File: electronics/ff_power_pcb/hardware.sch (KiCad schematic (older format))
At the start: 60 parts, among them J1 Conn_01x01_Female, J2 Conn_01x01_Female, J3 Conn_01x07_Male, U3 TPS62095RGTR, U4 TPS62095RGTR, U5 TPS62095RGTR, U6 TPS62095RGTR, U7 AP131-25

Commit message: Working on the electronics for the FF revision.
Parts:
- CY3: renamed from C3; footprint (none) -> Capacitor_THT:C_Disc_D7.5mm_W5.0mm_P10.00mm; MPN (none) -> C901U102MUVDBA7317
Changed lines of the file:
@@
 AR Path="/60536DA4/60E826A4" Ref="C?"  Part="1"
 AR Path="/60A30BFF/60E826A4" Ref="C?"  Part="1"
-AR Path="/60E826A4" Ref="C3"  Part="1"
-F 0 "C3" V 7950 2700 50  0000 L CNN
+AR Path="/60E826A4" Ref="CY3"  Part="1"
+F 0 "CY3" V 7950 2700 50  0000 L CNN
 F 1 "1.0nF" V 7900 3050 50  0000 C CNN
-F 2 "" H 8050 2850 50  0001 C CNN
+F 2 "Capacitor_THT:C_Disc_D7.5mm_W5.0mm_P10.00mm" H 8050 2850 50  0001 C CNN
 F 3 "~" H 8050 2850 50  0001 C CNN
-F 4 "" H 8100 3050 50  0001 C CNN "MPN"
+F 4 "C901U102MUVDBA7317" H 8100 3050 50  0001 C CNN "MPN"
 F 5 "~" H 8100 3050 50  0001 C CNN "Tolerance"
 F 6 "400Vac" V 8000 3050 50  0000 C CNN "Voltage"

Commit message: Added step files, Working on the power board.
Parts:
- F1: footprint Fuse:Fuse_Littelfuse-NANO2-451_453 -> Fuse:Fuse_Littelfuse_395Series; MPN 0679H1000-01 -> 36911000000
- J1, J2: footprint Connector_PinHeader_2.54mm:PinHeader_1x01_P2.54mm_Vertical -> mains_blade:IRL_00
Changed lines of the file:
@@
 F 0 "F1" V 5153 1950 50  0000 C CNN
 F 1 "1A/300V Slow" V 5244 1950 50  0000 C CNN
-F 2 "Fuse:Fuse_Littelfuse-NANO2-451_453" V 5280 1950 50  0001 C CNN
+F 2 "Fuse:Fuse_Littelfuse_395Series" V 5280 1950 50  0001 C CNN
 F 3 "~" H 5350 1950 50  0001 C CNN
-F 4 "0679H1000-01" V 5350 1950 50  0001 C CNN "MPN"
+F 4 "36911000000" V 5350 1950 50  0001 C CNN "MPN"
 	1    5350 1950
 	0    1    1    0
@@
 F 0 "J1" H 4142 2317 50  0000 C CNN
 F 1 "Conn_01x01_Female" H 4142 2316 50  0001 C CNN
-F 2 "Connector_PinHeader_2.54mm:PinHeader_1x01_P2.54mm_Vertical" H 4250 2450 50  0001 C CNN
+F 2 "mains_blade:IRL_00" H 4250 2450 50  0001 C CNN
 F 3 "~" H 4250 2450 50  0001 C CNN
 	1    4250 2450
@@
 F 0 "J2" H 4142 1817 50  0000 C CNN
 F 1 "Conn_01x01_Female" H 4142 1816 50  0001 C CNN
-F 2 "Connector_PinHeader_2.54mm:PinHeader_1x01_P2.54mm_Vertical" H 4250 1950 50  0001 C CNN
+F 2 "mains_blade:IRL_00" H 4250 1950 50  0001 C CNN
 F 3 "~" H 4250 1950 50  0001 C CNN
 	1    4250 1950

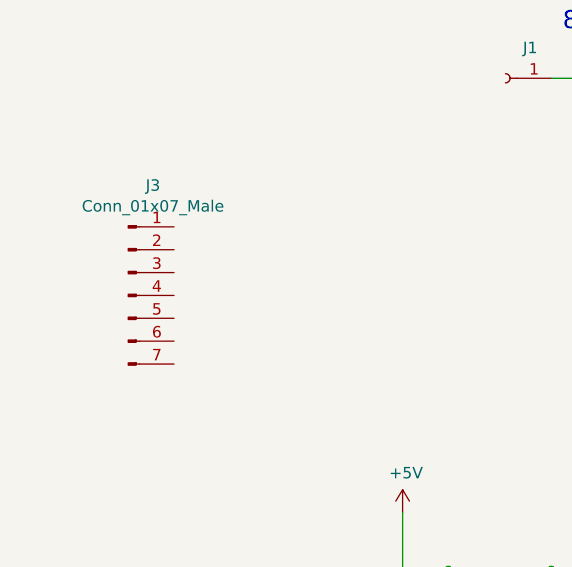
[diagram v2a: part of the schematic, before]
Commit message: Finished up the routing on the power board, still needs a double check.
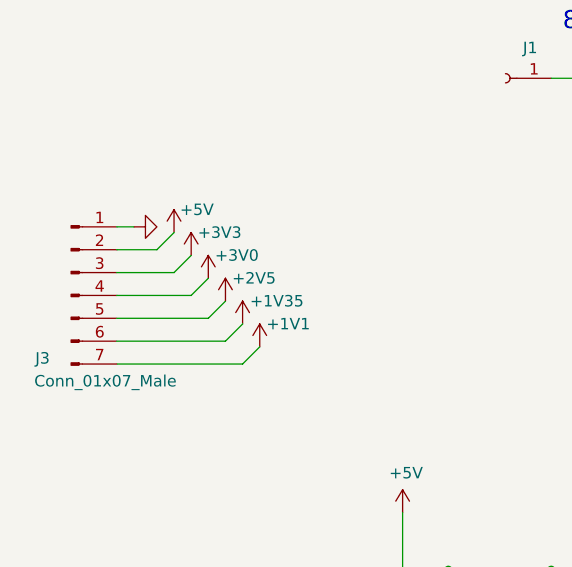
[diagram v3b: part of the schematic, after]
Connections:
- net +1V1: now also J3.7 (Pin_7)
- net +1V35: now also J3.6 (Pin_6)
- net +2V5: now also J3.5 (Pin_5)
- net +3V0: now also J3.4 (Pin_4)
- net +3V3: now also J3.3 (Pin_3)
- net +5V: now also J3.2 (Pin_2)
- net GND: now also J3.1 (Pin_1)
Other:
- moved on the sheet: J3
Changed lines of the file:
@@
 L Connector:Conn_01x07_Male J3
 U 1 1 60CBBBFE
-P 2600 3400
-F 0 "J3" H 2708 3881 50  0000 C CNN
-F 1 "Conn_01x07_Male" H 2708 3790 50  0000 C CNN
-F 2 "Connector_PinSocket_2.54mm:PinSocket_1x07_P2.54mm_Vertical" H 2600 3400 50  0001 C CNN
-F 3 "~" H 2600 3400 50  0001 C CNN
-	1    2600 3400
+P 2350 3400
+F 0 "J3" H 2225 3125 50  0000 C CNN
+F 1 "Conn_01x07_Male" H 2500 3025 50  0000 C CNN
+F 2 "Connector_PinSocket_2.54mm:PinSocket_1x07_P2.54mm_Vertical" H 2350 3400 50  0001 C CNN
+F 3 "~" H 2350 3400 50  0001 C CNN
+	1    2350 3400
 	1    0    0    -1
 $EndComp
@@
 Wire Wire Line
 	7050 1950 7450 1950
+Wire Wire Line
+	2550 3700 3100 3700
+Wire Wire Line
+	3100 3700 3175 3625
+$Comp
+L power:+1V35 #PWR?
+U 1 1 61108D89
+P 3100 3525
+AR Path="/60536DA4/61108D89" Ref="#PWR?"  Part="1"
+AR Path="/60A30BFF/61108D89" Ref="#PWR?"  Part="1"
+AR Path="/61108D89" Ref="#PWR?"  Part="1"
+F 0 "#PWR?" H 3100 3375 50  0001 C CNN
+F 1 "+1V35" H 3250 3625 50  0000 C CNN
+F 2 "" H 3100 3525 50  0001 C CNN
+F 3 "" H 3100 3525 50  0001 C CNN
+	1    3100 3525
+	1    0    0    -1
+$EndComp
+$Comp
+L power:+5V #PWR?
+U 1 1 6110AA8A
+P 2800 3125
+F 0 "#PWR?" H 2800 2975 50  0001 C CNN
+F 1 "+5V" H 2900 3225 50  0000 C CNN
+F 2 "" H 2800 3125 50  0001 C CNN
+F 3 "" H 2800 3125 50  0001 C CNN
+	1    2800 3125
+	1    0    0    -1
+$EndComp
+$Comp
+L power:+3V0 #PWR?
+U 1 1 6110CD65
+P 2950 3325
+F 0 "#PWR?" H 2950 3175 50  0001 C CNN
+F 1 "+3V0" H 3075 3425 50  0000 C CNN
+F 2 "" H 2950 3325 50  0001 C CNN
+F 3 "" H 2950 3325 50  0001 C CNN
+	1    2950 3325
+	1    0    0    -1
+$EndComp
+$Comp
+L power:+1V1 #PWR?
+U 1 1 611106CE
+P 3175 3625
+F 0 "#PWR?" H 3175 3475 50  0001 C CNN
+F 1 "+1V1" H 3300 3725 50  0000 C CNN
+F 2 "" H 3175 3625 50  0001 C CNN
+F 3 "" H 3175 3625 50  0001 C CNN
+	1    3175 3625
+	1    0    0    -1
+$EndComp
+$Comp
+L power:+2V5 #PWR?
+U 1 1 61112D49
+P 3025 3425
+F 0 "#PWR?" H 3025 3275 50  0001 C CNN
+F 1 "+2V5" H 3150 3525 50  0000 C CNN
+F 2 "" H 3025 3425 50  0001 C CNN
+F 3 "" H 3025 3425 50  0001 C CNN
+	1    3025 3425
+	1    0    0    -1
+$EndComp
+Wire Wire Line
+	2550 3600 3025 3600
+Wire Wire Line
+	3025 3600 3100 3525
+Wire Wire Line
+	2550 3500 2950 3500
+Wire Wire Line
+	2950 3500 3025 3425
+Wire Wire Line
+	2550 3400 2875 3400
+Wire Wire Line
+	2875 3400 2950 3325
+Wire Wire Line
+	2550 3300 2800 3300
+Wire Wire Line
+	2800 3300 2875 3225
+$Comp
+L power:+3V3 #PWR?
+U 1 1 61107094
+P 2875 3225
+F 0 "#PWR?" H 2875 3075 50  0001 C CNN
+F 1 "+3V3" H 3000 3325 50  0000 C CNN
+F 2 "" H 2875 3225 50  0001 C CNN
+F 3 "" H 2875 3225 50  0001 C CNN
+	1    2875 3225
+	1    0    0    -1
+$EndComp
+Wire Wire Line
+	2550 3200 2725 3200
+Wire Wire Line
+	2725 3200 2800 3125
+$Comp
+L power:GND #PWR?
+U 1 1 61381F70
+P 2625 3100
+AR Path="/60536DA4/61381F70" Ref="#PWR?"  Part="1"
+AR Path="/60A30BFF/61381F70" Ref="#PWR?"  Part="1"
+AR Path="/61381F70" Ref="#PWR?"  Part="1"
+F 0 "#PWR?" H 2625 2850 50  0001 C CNN
+F 1 "GND" V 2630 2972 50  0001 R CNN
+F 2 "" H 2625 3100 50  0001 C CNN
+F 3 "" H 2625 3100 50  0001 C CNN
+	1    2625 3100
+	0    -1   -1   0
+$EndComp
+Wire Wire Line
+	2625 3100 2550 3100
 $EndSCHEMATC

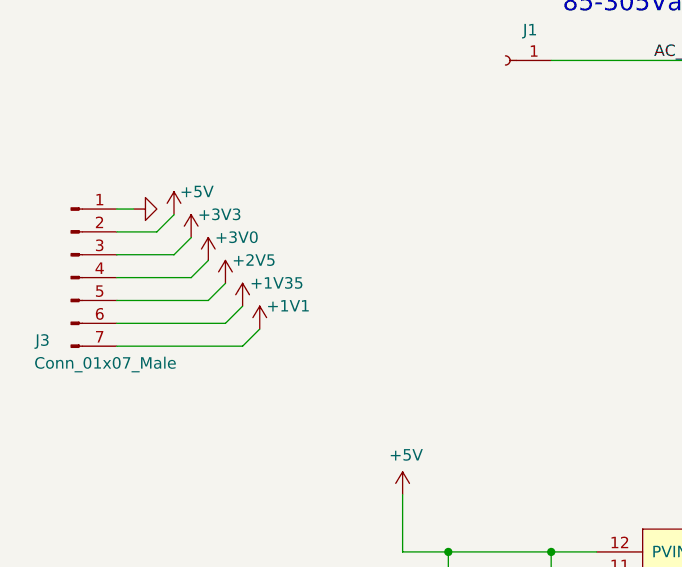
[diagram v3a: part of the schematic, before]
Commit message: Rerouted the power traces for R0.1 power pcb - they didn't match the compute PCB power pins.
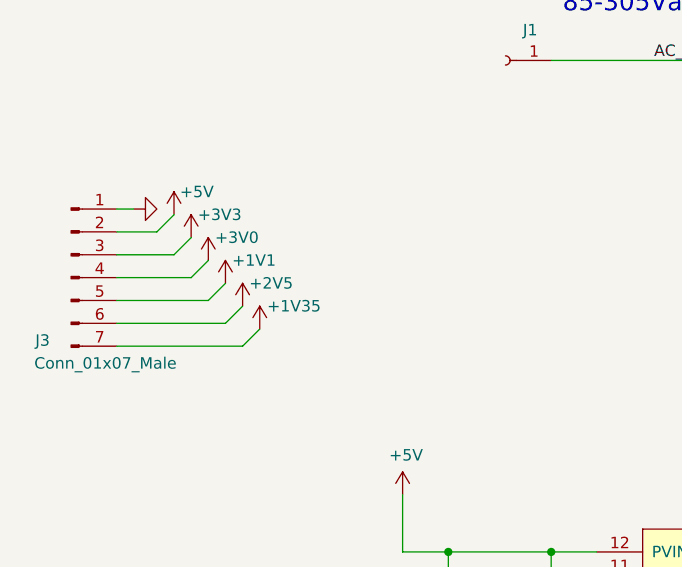
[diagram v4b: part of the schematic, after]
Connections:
- net +1V1: now also J3.5 (Pin_5); no longer J3.7 (Pin_7)
- net +1V35: now also J3.7 (Pin_7); no longer J3.6 (Pin_6)
- net +2V5: now also J3.6 (Pin_6); no longer J3.5 (Pin_5)
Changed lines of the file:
@@
 L power:+1V35 #PWR?
 U 1 1 61108D89
-P 3100 3525
+P 3175 3625
 AR Path="/60536DA4/61108D89" Ref="#PWR?"  Part="1"
 AR Path="/60A30BFF/61108D89" Ref="#PWR?"  Part="1"
 AR Path="/61108D89" Ref="#PWR?"  Part="1"
-F 0 "#PWR?" H 3100 3375 50  0001 C CNN
-F 1 "+1V35" H 3250 3625 50  0000 C CNN
-F 2 "" H 3100 3525 50  0001 C CNN
-F 3 "" H 3100 3525 50  0001 C CNN
-	1    3100 3525
+F 0 "#PWR?" H 3175 3475 50  0001 C CNN
+F 1 "+1V35" H 3325 3725 50  0000 C CNN
+F 2 "" H 3175 3625 50  0001 C CNN
+F 3 "" H 3175 3625 50  0001 C CNN
+	1    3175 3625
 	1    0    0    -1
 $EndComp
@@
 L power:+1V1 #PWR?
 U 1 1 611106CE
-P 3175 3625
-F 0 "#PWR?" H 3175 3475 50  0001 C CNN
-F 1 "+1V1" H 3300 3725 50  0000 C CNN
-F 2 "" H 3175 3625 50  0001 C CNN
-F 3 "" H 3175 3625 50  0001 C CNN
-	1    3175 3625
-	1    0    0    -1
-$EndComp
-$Comp
-L power:+2V5 #PWR?
-U 1 1 61112D49
 P 3025 3425
 F 0 "#PWR?" H 3025 3275 50  0001 C CNN
-F 1 "+2V5" H 3150 3525 50  0000 C CNN
+F 1 "+1V1" H 3150 3525 50  0000 C CNN
 F 2 "" H 3025 3425 50  0001 C CNN
 F 3 "" H 3025 3425 50  0001 C CNN
@@
 Wire Wire Line
 	2625 3100 2550 3100
+$Comp
+L power:+2V5 #PWR?
+U 1 1 61112D49
+P 3100 3525
+F 0 "#PWR?" H 3100 3375 50  0001 C CNN
+F 1 "+2V5" H 3225 3625 50  0000 C CNN
+F 2 "" H 3100 3525 50  0001 C CNN
+F 3 "" H 3100 3525 50  0001 C CNN
+	1    3100 3525
+	1    0    0    -1
+$EndComp
 $EndSCHEMATC

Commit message: Updated the regulator to the proper value.
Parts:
- U7: value AP131-25 -> AP131-33; symbol Regulator_Linear:AP131-25 -> Regulator_Linear:AP131-33; MPN AP131-25 -> AP131-33
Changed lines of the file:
@@
 $EndComp
 $Comp
-L Regulator_Linear:AP131-25 U7
+L Regulator_Linear:AP131-33 U7
 U 1 1 60A041CF
 P 8350 9350
 F 0 "U7" H 8350 9692 50  0000 C CNN
-F 1 "AP131-25" H 8350 9601 50  0000 C CNN
+F 1 "AP131-33" H 8350 9601 50  0000 C CNN
 F 2 "Package_TO_SOT_SMD:SOT-23-5" H 8350 9675 50  0001 C CNN
 F 3 "~" H 8350 9350 50  0001 C CNN
-F 4 "AP131-25" H 8350 9350 50  0001 C CNN "MPN"
+F 4 "AP131-33" H 8350 9350 50  0001 C CNN "MPN"
 F 5 "~" H 8350 9792 50  0001 C CNN "Tolerance"
 	1    8350 9350

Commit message: Revert
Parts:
- U7: value AP131-33 -> AP131-25; symbol Regulator_Linear:AP131-33 -> Regulator_Linear:AP131-25; MPN AP131-33 -> AP131-25
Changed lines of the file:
@@
 $EndComp
 $Comp
-L Regulator_Linear:AP131-33 U7
+L Regulator_Linear:AP131-25 U7
 U 1 1 60A041CF
 P 8350 9350
 F 0 "U7" H 8350 9692 50  0000 C CNN
-F 1 "AP131-33" H 8350 9601 50  0000 C CNN
+F 1 "AP131-25" H 8350 9601 50  0000 C CNN
 F 2 "Package_TO_SOT_SMD:SOT-23-5" H 8350 9675 50  0001 C CNN
 F 3 "~" H 8350 9350 50  0001 C CNN
-F 4 "AP131-33" H 8350 9350 50  0001 C CNN "MPN"
+F 4 "AP131-25" H 8350 9350 50  0001 C CNN "MPN"
 F 5 "~" H 8350 9792 50  0001 C CNN "Tolerance"
 	1    8350 9350
